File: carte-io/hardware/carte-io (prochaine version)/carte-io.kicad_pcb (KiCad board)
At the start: 4 copper layers, 117.5 x 88.5 mm, 191 parts, among them J1 USB_C_Receptacle_USB2.0_14P, J10 JST_PH_B4B, J11 JST_PH_B4B, J12 JST_PH_B4B, J13 JST_PH_B4B, J14 JST_PH_B4B, J15 JST_PH_B4B, J16 JST_PH_B4B, J17 JST_PH_B4B, J18 JST_PH_B4B, J19 JST_PH_B4B, J2 JST-XH_S2B-XH-A, J20 Conn_02x08_Odd_Even, J22 JST_PH_B6B, J23 JST_PH_B4B, J24 JST_PH_B4B, J25 JST_PH_B4B, J26 JST-PH-B2B, J27 JST_PH_B5B, J3 FTSH-105-01-L-DV-007, J4 JST_PH_B4B, J5 JST_PH_B4B, J6 JST_PH_B4B, J7 JST_PH_B4B, J8 TSW-104-07-G-T, J9 TSW-104-07-G-T, Q1 IRF9388TRPBF, SW1 SW_Push, SW2 SW_Push, U1 STM32U545VETx, U10 CM1293A-04SO, U11 74LVC125APW, U12 LSM6DS3, U13 LIS2MDL, U14 LPS22DF, U15 PCA9544APW, U16 LT1963AxST-3.3, U17 PCA9544APW, U18 APDS-9251-001, U19 SHT4x, U2 FT231XQ, U20 74LVC2G125DP,125, U21 CM1293A-04SO, U22 CM1293A-04SO, U23 74LVC125APW, U24 CM1293A-04SO, U25 74LVC125APW, U26 74LVC2G125DP,125, U27 CM1293A-04SO, U28 74LVC2G125DP,125, U29 CM1293A-04SO, U3 LT1963AxST-3.3, U30 74LVC125APW,118, U31 CM1293A-04SO, U32 74LVC2G125DP,125, U33 MCP2542FDxMF, U34 CM1293A-04SO, U35 TCA9802, U4 CM1293A-04SO, U5 TXU0104PWR, U6 74LVC125APW, U7 CM1293A-04SO, U8 CM1293A-04SO, U9 TXU0104PWR, X1 ASE-16.000MHZ-LC-T

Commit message: Commit de sauvegarde, gros changement sur la carte IO, les connecteurs sont compatibles SeeedStudio Grove. Il faut reprendre une grosse partie du routage et rajouter deux entrées analogiques
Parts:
- removed C39, C40, C41, C43: 100nF, Capacitor_SMD:C_0805_2012Metric_Pad1.18x1.45mm_HandSolder
- removed R36, R37, R38, R39, R44, R47, R48, R49: 100R, Resistor_SMD:R_0805_2012Metric_Pad1.20x1.40mm_HandSolder
- removed U22, U31: CM1293A-04SO, CM1293A-04SO:SOT95P285X140-6N
- removed U23, U25: 74LVC125APW, 74LVC125APW:IC_74LVC125APW
- removed U30: 74LVC125APW,118, Package_SO:TSSOP-14_4.4x5mm_P0.65mm
- added J21: 114020164, SeeedStudio - Horizontal Header -114020164:SEEEDSTUDIO_114020164, F.Cu at (179.0, 155.6)
- added J28: 114020164, SeeedStudio - Horizontal Header -114020164:SEEEDSTUDIO_114020164, F.Cu at (204.1, 155.6)
- added R73: 4.7K, Resistor_SMD:R_0805_2012Metric_Pad1.20x1.40mm_HandSolder, F.Cu at (216.8, 57.8)
- added R74: 4.7K, Resistor_SMD:R_0805_2012Metric_Pad1.20x1.40mm_HandSolder, F.Cu at (216.8, 60.7)
- J10, J12, J14, J16, J18, J19, J23, J24, J25, J4, J5, J6, J7: value JST_PH_B4B -> 114020164; footprint Connector_JST:JST_PH_B4B-PH-K_1x04_P2.00mm_Vertical -> SeeedStudio - Horizontal Header -114020164:SEEEDSTUDIO_114020164
- J11, J13, J15, J17: value JST_PH_B4B -> 114020164; footprint Connector_JST:JST_PH_B4B-PH-K_1x04_P2.00mm_Vertical -> SeeedStudio - Horizontal Header -114020164:SEEEDSTUDIO_114020164; moved to B.Cu
- J2: value JST-XH_S2B-XH-A -> 114020164; footprint Connector_JST:JST_XH_S2B-XH-A_1x02_P2.50mm_Horizontal -> SeeedStudio - Horizontal Header -114020164:SEEEDSTUDIO_114020164
- J20: value Conn_02x08_Odd_Even -> 114020164; footprint Connector_PinHeader_2.54mm:PinHeader_2x07_P2.54mm_Vertical -> SeeedStudio - Horizontal Header -114020164:SEEEDSTUDIO_114020164
- J22: value JST_PH_B6B -> 114020164; footprint Connector_JST:JST_PH_B6B-PH-K_1x06_P2.00mm_Vertical -> SeeedStudio - Horizontal Header -114020164:SEEEDSTUDIO_114020164
- J26: value JST-PH-B2B -> 114020164; footprint Connector_JST:JST_PH_B2B-PH-K_1x02_P2.00mm_Vertical -> SeeedStudio - Horizontal Header -114020164:SEEEDSTUDIO_114020164; moved to B.Cu
- J27: value JST_PH_B5B -> 114020164; footprint Connector_JST:JST_PH_B5B-PH-K_1x05_P2.00mm_Vertical -> SeeedStudio - Horizontal Header -114020164:SEEEDSTUDIO_114020164
- moved J22 51.7 mm to (191.6, 155.6), turned to 90 degrees
- moved J26 42.1 mm to (92.7, 124.2), turned to 90 degrees
- moved J20 19.7 mm to (166.5, 155.6)
- moved J12 7.32 mm to (144.3, 60.4), turned to 180 degrees
- moved J16 7.32 mm to (157.0, 60.4), turned to 180 degrees
- moved J14 7.11 mm to (131.3, 60.4), turned to 180 degrees
- moved J10 6.74 mm to (118.0, 60.4), turned to 180 degrees
- moved J15 6.19 mm to (130.9, 60.2), turned to 0 degrees
- moved J11 6.13 mm to (117.8, 60.4), turned to 0 degrees
- moved J13 5.96 mm to (144.4, 60.2), turned to 0 degrees
- moved U19 5.96 mm to (169.8, 85.5)
- moved J17 5.63 mm to (157.2, 60.5), turned to 0 degrees
- moved J2 2.95 mm to (92.7, 124.2)
- moved R29 1.63 mm to (164.1, 85.3)
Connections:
- J10 pad 1: +3.3V_PWR -> Net-(J10-Pin_1)
- J10 pad 3: GND -> +3.3V_PWR
- J10 pad 4: Net-(J10-Pin_4) -> GND
- J11 pad 1: +3.3V_PWR -> Net-(J11-Pin_1)
- J11 pad 3: GND -> +3.3V_PWR
- J11 pad 4: Net-(J11-Pin_4) -> GND
- J12 pad 1: +3.3V_PWR -> Net-(J12-Pin_1)
- J12 pad 3: GND -> +3.3V_PWR
- J12 pad 4: Net-(J12-Pin_4) -> GND
- J13 pad 1: +3.3V_PWR -> Net-(J13-Pin_1)
- J13 pad 3: GND -> +3.3V_PWR
- J13 pad 4: Net-(J13-Pin_4) -> GND
- J14 pad 1: +3.3V_PWR -> Net-(J14-Pin_1)
- J14 pad 3: GND -> +3.3V_PWR
- J14 pad 4: Net-(J14-Pin_4) -> GND
- J15 pad 1: +3.3V_PWR -> Net-(J15-Pin_1)
- J15 pad 3: GND -> +3.3V_PWR
- J15 pad 4: Net-(J15-Pin_4) -> GND
- J16 pad 1: +3.3V_PWR -> Net-(J16-Pin_1)
- J16 pad 3: GND -> +3.3V_PWR
- J16 pad 4: Net-(J16-Pin_4) -> GND
- J17 pad 1: +3.3V_PWR -> Net-(J17-Pin_1)
- J17 pad 3: GND -> +3.3V_PWR
- J17 pad 4: Net-(J17-Pin_4) -> GND
- J18 pad 1: +5V -> Net-(J18-Pin_1)
- J18 pad 3: GND -> +5V
- J18 pad 4: Net-(J18-Pin_4) -> GND
- J19 pad 1: +5V -> Net-(J19-Pin_1)
- J19 pad 3: GND -> +5V
- J19 pad 4: Net-(J19-Pin_4) -> GND
- J2 pad 1: /Power & Analog/VIN -> GND
- J2 pad 2: GND -> /Power & Analog/VIN
- J20 pad 1: +3.3V_PWR -> /GPIO SPI GEN_PWM/IO1
- J20 pad 2: +5V -> unconnected-(J20-Pin_2-Pad2)
- J20 pad 3: GND -> +3.3V
- J22 pad 1: +3.3V_PWR -> /GPIO SPI GEN_PWM/IO4
- J22 pad 2: /GPIO SPI GEN_PWM/SPI_CS_EXT -> unconnected-(J22-Pin_2-Pad2)
- J22 pad 3: /GPIO SPI GEN_PWM/SPI_CLK_EXT -> +3.3V
- J23 pad 1: +3.3V_PWR -> Net-(J23-Pin_1)
- J23 pad 3: GND -> +3.3V_PWR
- J23 pad 4: Net-(J23-Pin_4) -> GND
- J24 pad 1: +3.3V_PWR -> Net-(J23-Pin_1)
- J24 pad 3: GND -> +3.3V_PWR
- J24 pad 4: Net-(J23-Pin_4) -> GND
- J25 pad 1: +5V -> Net-(J25-Pin_1)
- J25 pad 3: GND -> +5V
- J25 pad 4: Net-(J25-Pin_4) -> GND
- J26 pad 1: GND -> /CPU/~{POWEROFF}
- J26 pad 2: Net-(J26-Pin_2) -> /CPU/PWR_CSLEEP
- J27 pad 1: +5V -> Net-(J27-Pin_1)
- J27 pad 2: +3.3V -> Net-(J27-Pin_2)
- J27 pad 3: Net-(J27-Pin_3) -> +5V
- J4 pad 1: +3.3V -> Net-(J4-Pin_1)
- J4 pad 3: GND -> +3.3V
- J4 pad 4: Net-(J4-Pin_4) -> GND
- J5 pad 1: +3.3V -> Net-(J5-Pin_1)
- J5 pad 3: GND -> +3.3V
- J5 pad 4: Net-(J5-Pin_4) -> GND
- J6 pad 1: +3.3V -> Net-(J6-Pin_1)
- J6 pad 3: GND -> +3.3V
- J6 pad 4: Net-(J6-Pin_4) -> GND
- J7 pad 1: +3.3V -> Net-(J7-Pin_1)
- J7 pad 3: GND -> +3.3V
- J7 pad 4: Net-(J7-Pin_4) -> GND
- R11 pad 1: Net-(J4-Pin_2) -> Net-(J4-Pin_1)
- R12 pad 1: Net-(J4-Pin_4) -> Net-(J4-Pin_2)
- R13 pad 1: Net-(J5-Pin_2) -> Net-(J5-Pin_1)
- R14 pad 1: Net-(J5-Pin_4) -> Net-(J5-Pin_2)
- R19 pad 1: Net-(J6-Pin_2) -> Net-(J6-Pin_1)
- R20 pad 1: Net-(J6-Pin_4) -> Net-(J6-Pin_2)
- R21 pad 1: Net-(J7-Pin_2) -> Net-(J7-Pin_1)
- R22 pad 1: Net-(J7-Pin_4) -> Net-(J7-Pin_2)
- R32 pad 2: Net-(J18-Pin_4) -> Net-(J18-Pin_1)
- R34 pad 2: Net-(J19-Pin_4) -> Net-(J19-Pin_1)
- R35 pad 2: Net-(J25-Pin_4) -> Net-(J25-Pin_1)
- R40 pad 1: Net-(U23-1Y) -> /CPU/IO1
- R40 pad 2: /GPIO SPI GEN_PWM/OUT1 -> /GPIO SPI GEN_PWM/IO1
- R41 pad 1: Net-(U23-2Y) -> /CPU/IO2
- R41 pad 2: /GPIO SPI GEN_PWM/OUT2 -> /GPIO SPI GEN_PWM/IO2
- R42 pad 1: Net-(U23-3Y) -> /CPU/IO3
- R42 pad 2: /GPIO SPI GEN_PWM/OUT3 -> /GPIO SPI GEN_PWM/IO3
- R43 pad 1: Net-(U23-4Y) -> /CPU/IO4
- R43 pad 2: /GPIO SPI GEN_PWM/OUT4 -> /GPIO SPI GEN_PWM/IO4
- R45 pad 2: Net-(J27-Pin_3) -> Net-(J27-Pin_2)
- R46 pad 2: Net-(J27-Pin_5) -> Net-(J27-Pin_1)
- R52 pad 1: Net-(J26-Pin_2) -> Net-(J26-Pin_3)
- R57 pad 2: Net-(J10-Pin_4) -> Net-(J10-Pin_1)
- R59 pad 2: Net-(J14-Pin_4) -> Net-(J14-Pin_1)
- R61 pad 2: Net-(J15-Pin_4) -> Net-(J15-Pin_1)
- R62 pad 1: Net-(J11-Pin_4) -> Net-(J11-Pin_1)
- R65 pad 2: Net-(J12-Pin_4) -> Net-(J12-Pin_1)
- R67 pad 2: Net-(J16-Pin_4) -> Net-(J16-Pin_1)
- R69 pad 2: Net-(J17-Pin_4) -> Net-(J17-Pin_1)
- R70 pad 1: Net-(J13-Pin_4) -> Net-(J13-Pin_1)
- U1 pad 31: /CPU/SPI_MISO -> unconnected-(U1-PA6-Pad31)
- U1 pad 32: /CPU/SPI_MOSI -> unconnected-(U1-PA7-Pad32)
- U1 pad 38: /CPU/INPUT1 -> /CPU/IO1
- U1 pad 39: /CPU/INPUT2 -> /CPU/IO2
- U1 pad 40: /CPU/INPUT3 -> /CPU/IO3
- U1 pad 41: /CPU/INPUT4 -> /CPU/IO4
- U1 pad 42: /CPU/OUTPUT1 -> unconnected-(U1-PE11-Pad42)
- U1 pad 43: /CPU/OUTPUT2 -> unconnected-(U1-PE12-Pad43)
- U1 pad 44: /CPU/SPI_SCK -> unconnected-(U1-PE13-Pad44)
- U1 pad 45: /CPU/OUTPUT3 -> unconnected-(U1-PE14-Pad45)
- U1 pad 46: /CPU/OUTPUT4 -> unconnected-(U1-PE15-Pad46)
- U1 pad 97: /CPU/SPI_CS -> unconnected-(U1-PE0-Pad97)
- U15 pad 13: Net-(J11-Pin_4) -> Net-(J11-Pin_1)
- U15 pad 16: Net-(J15-Pin_4) -> Net-(J15-Pin_1)
- U15 pad 6: Net-(J10-Pin_4) -> Net-(J10-Pin_1)
- U15 pad 9: Net-(J14-Pin_4) -> Net-(J14-Pin_1)
- U17 pad 13: Net-(J13-Pin_4) -> Net-(J13-Pin_1)
- U17 pad 16: Net-(J17-Pin_4) -> Net-(J17-Pin_1)
- U17 pad 6: Net-(J12-Pin_4) -> Net-(J12-Pin_1)
- U17 pad 9: Net-(J16-Pin_4) -> Net-(J16-Pin_1)
- U21 pad 5: +5V -> +3.3V
- U24 pad 1: Net-(U23-1Y) -> /CPU/IO1
- U24 pad 3: Net-(U23-2Y) -> /CPU/IO2
- U24 pad 4: Net-(U23-3Y) -> /CPU/IO3
- U24 pad 6: Net-(U23-4Y) -> /CPU/IO4
- U27 pad 5: +5V -> +3.3V
- U29 pad 5: +5V -> +3.3V
- U33 pad 6: Net-(J25-Pin_4) -> Net-(J25-Pin_1)
- U35 pad 7: Net-(J23-Pin_4) -> Net-(J23-Pin_1)
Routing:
- net (no net): track 0.00 -> 326.6 mm, vias 0 -> 9
- net /CPU/IO4: track 0.00 -> 88.5 mm, vias 0 -> 5
- net /CPU/IO2: track 0.00 -> 85.8 mm, vias 0 -> 2
- net /CPU/IO3: track 0.00 -> 85.3 mm, vias 0 -> 5
- net /CPU/IO1: track 0.00 -> 83.1 mm, vias 0 -> 4
- net GND: track 447.9 -> 530.1 mm, vias 63 -> 70
- net unconnected-(U1-PA6-Pad31): track 0.00 -> 57.4 mm, vias 0 -> 4
- net /CPU/SPI_MISO: track 57.4 -> 0.00 mm, vias 4 -> 0
- net /CPU/INPUT2: track 56.9 -> 0.00 mm, vias 2 -> 0
- net /CPU/INPUT1: track 55.2 -> 0.00 mm, vias 2 -> 0
- net unconnected-(U1-PE0-Pad97): track 0.00 -> 54.8 mm, vias 0 -> 4
- net /CPU/SPI_CS: track 54.8 -> 0.00 mm, vias 4 -> 0
- net /CPU/INPUT3: track 52.3 -> 0.00 mm, vias 2 -> 0
- net unconnected-(U1-PA7-Pad32): track 0.00 -> 51.3 mm, vias 0 -> 4
- net /CPU/SPI_MOSI: track 51.3 -> 0.00 mm, vias 4 -> 0
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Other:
- outline, holes or cut-outs redrawn

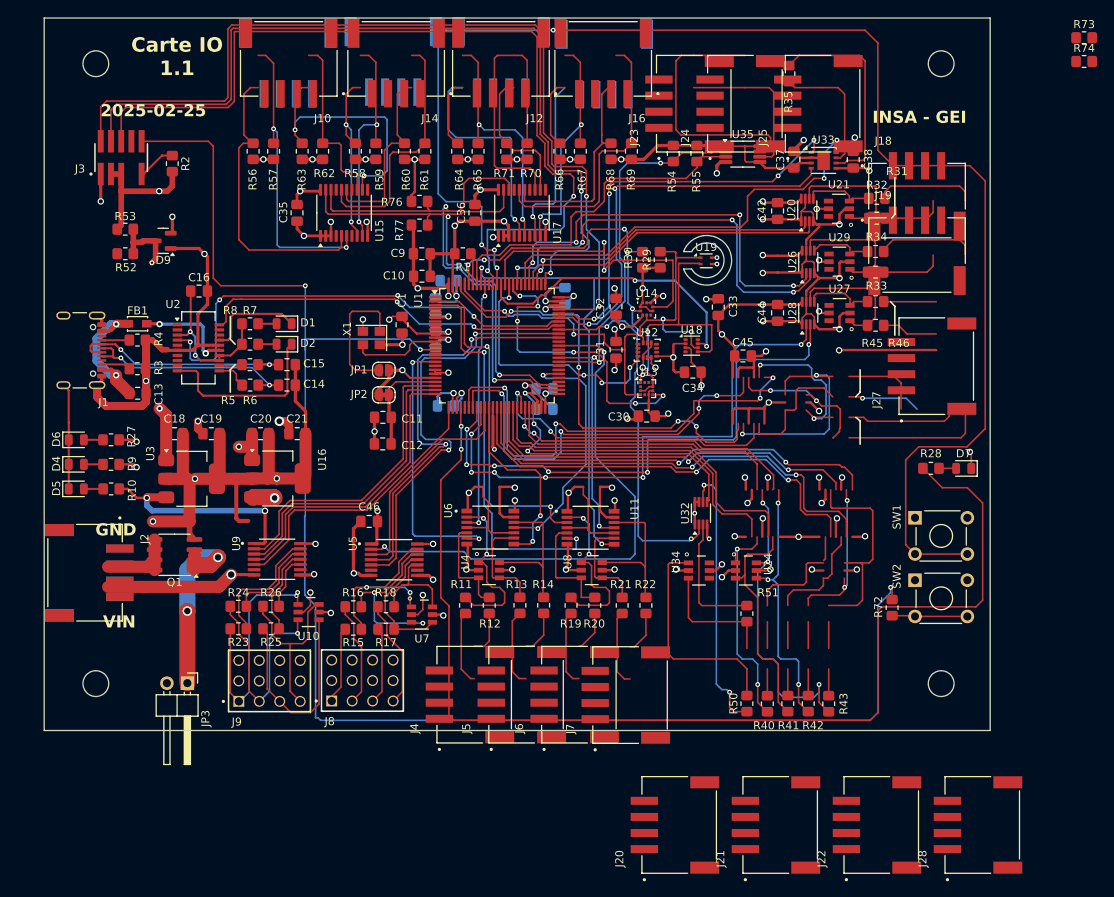
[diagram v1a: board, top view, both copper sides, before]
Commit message: -- reorganisation de la carte, - rajout des connecteurs seeedstudio grove - Rajout des deux entrées ADC
travail en cours
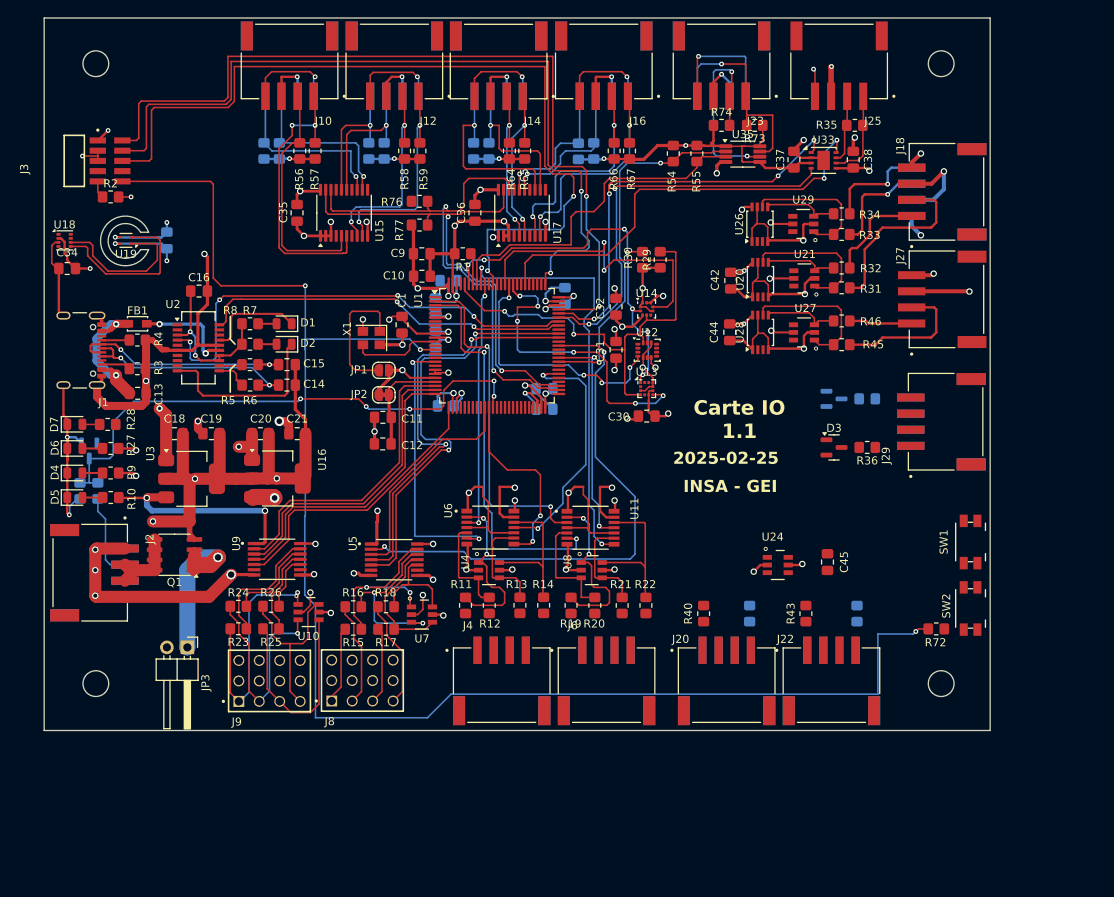
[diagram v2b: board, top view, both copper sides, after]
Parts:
- removed C46: 100nF, Capacitor_SMD:C_0805_2012Metric_Pad1.18x1.45mm_HandSolder
- removed R50, R51: 100R, Resistor_SMD:R_0805_2012Metric_Pad1.20x1.40mm_HandSolder
- removed U32: 74LVC2G125DP,125, Package_SO:VSSOP-8_2.3x2mm_P0.5mm
- removed U34: CM1293A-04SO, CM1293A-04SO:SOT95P285X140-6N
- added D3: BAT54SFILMY, Package_TO_SOT_SMD:SOT-23, F.Cu at (185.7, 108.7)
- added D8: BAT54SFILMY, Package_TO_SOT_SMD:SOT-23, B.Cu at (185.7, 102.6)
- added J29: 114020164, SeeedStudio - Horizontal Header -114020164:SEEEDSTUDIO_114020164, F.Cu at (199.5, 105.5)
- added J30: 114020164, SeeedStudio - Horizontal Header -114020164:SEEEDSTUDIO_114020164, B.Cu at (199.5, 105.5)
- added R36: 100R, Resistor_SMD:R_0805_2012Metric_Pad1.20x1.40mm_HandSolder, F.Cu at (189.8, 108.7)
- added R37: 100R, Resistor_SMD:R_0805_2012Metric_Pad1.20x1.40mm_HandSolder, B.Cu at (189.8, 102.6)
- C33, D9, J19, J21, J24, J28, J5, J7, R41, R42, R52, R53, R60, R61, R62, R63, R68, R69, R70, R71: moved to B.Cu
- J3: value FTSH-105-01-L-DV-007 -> FTSH-105-01-L-DH; footprint FTSH-105-01-L-DV-007-K:SAMTEC_FTSH-105-X-X-DV-007-P-X -> FTSH-105-01-L-DH:SAMTEC_FTSH-105-01-L-DH
- SW1, SW2: footprint Button_Switch_THT:SW_TH_Tactile_Omron_B3F-10xx -> Button_Switch_SMD:Panasonic_EVQPUJ_EVQPUA
- U20, U26, U28: footprint Package_SO:VSSOP-8_2.3x2mm_P0.5mm -> Package_SO:TSSOP-8_3x3mm_P0.65mm
- moved D7 110.5 mm to (91.4, 105.8), turned to 0 degrees
- moved R28 102.4 mm to (95.5, 105.8), turned to 180 degrees
- moved U18 79.0 mm to (90.1, 82.9)
- moved C34 78.8 mm to (90.4, 86.4), turned to 180 degrees
- moved U19 72.1 mm to (97.7, 82.9), turned to 180 degrees
- moved C33 69.0 mm to (102.8, 82.9), turned to -90 degrees
- moved R74 45.7 mm to (171.7, 68.7)
- moved R73 42.3 mm to (175.8, 68.7), turned to 180 degrees
- moved R53 33.0 mm to (92.0, 114.1), turned to -90 degrees
- moved R52 29.7 mm to (94.2, 114.1), turned to 90 degrees
- moved D9 27.7 mm to (93.2, 109.1), turned to -90 degrees
- moved C45 27.7 mm to (184.9, 122.9), turned to 90 degrees
- moved J28 25.5 mm to (185.4, 138.2), turned to 180 degrees
- moved J21 18.6 mm to (172.4, 138.2), turned to 180 degrees
- moved J22 18.4 mm to (185.4, 138.2), turned to 0 degrees
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- renumbered J14 to J12, J15 to J13, J12 to J14, J13 to J15
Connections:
- U1 pad 43: unconnected-(U1-PE12-Pad43) -> /CPU/ADC_AN1
- U1 pad 44: unconnected-(U1-PE13-Pad44) -> /CPU/ADC_AN2
- U1 pad 47: /CPU/GEN_PWM2 -> unconnected-(U1-PB10-Pad47)
- U1 pad 67: /CPU/GEN_PWM1 -> unconnected-(U1-PA8-Pad67)
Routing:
- net (no net): track 326.6 -> 0.00 mm, vias 9 -> 0
- net /CPU/USER_BTN: track 181.2 -> 0.00 mm, vias 4 -> 0
- net /CPU/LED_ACTIVITY: track 141.2 -> 0.00 mm, vias 2 -> 0
- net +3.3V_PWR: track 227.5 -> 125.0 mm, vias 3 -> 8
- net /CPU/IO4: track 88.5 -> 0.00 mm, vias 5 -> 0
- net /CPU/IO2: track 85.8 -> 0.00 mm, vias 2 -> 0
- net /CPU/IO3: track 85.3 -> 0.00 mm, vias 5 -> 0
- net /CPU/IO1: track 83.1 -> 0.00 mm, vias 4 -> 0
- net /CPU/COM_GPS_RX: track 68.6 -> 0.00 mm, vias 6 -> 0
- net GND: track 530.1 -> 461.7 mm, vias 70 -> 60
- net /CPU/COM_GPS_TX: track 68.3 -> 0.00 mm, vias 6 -> 0
- net unconnected-(U1-PA6-Pad31): track 57.4 -> 0.00 mm, vias 4 -> 0
- net unconnected-(U1-PE0-Pad97): track 54.8 -> 0.00 mm, vias 4 -> 0
- net /CPU/COM_LIDAR2_RX: track 52.7 -> 0.00 mm, vias 4 -> 0
- net /CPU/COM_LIDAR2_TX: track 51.4 -> 0.00 mm, vias 4 -> 0
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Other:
- outline, holes or cut-outs redrawn
- board text removed: "GND"
- board text removed: "VIN"

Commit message: WIP
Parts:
- added C43: 100nF, Capacitor_SMD:C_0805_2012Metric_Pad1.18x1.45mm_HandSolder, F.Cu at (172.7, 80.7)
- R13, R14, R21, R22: moved to B.Cu
- moved C45 6.92 mm to (178.7, 119.8), turned to 180 degrees
- moved R14 4.26 mm to (145.4, 128.3)
- moved R22 3.94 mm to (158.4, 128.3)
- moved C30 3.26 mm to (165.7, 104.8)
- moved C31 3.17 mm to (161.8, 96.5)
- moved C32 3.17 mm to (161.8, 91.2)
- moved R29 3.17 mm to (167.3, 85.3)
- moved R30 3.17 mm to (165.1, 85.3)
- moved U12 3.17 mm to (165.7, 96.6)
- moved U13 3.17 mm to (165.6, 101.4)
- moved U14 3.17 mm to (165.6, 91.5)
- moved R11 1.32 mm to (141.2, 128.3)
- moved R19 1.23 mm to (154.3, 128.3)
- moved R21 1.23 mm to (160.6, 128.3)
- moved R40 0.95 mm to (169.5, 128.3)
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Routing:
- net GND: track 461.7 -> 558.3 mm, vias 60 -> 78
- net /CPU/USER_BTN: track 0.00 -> 95.4 mm, vias 0 -> 4
- net +3.3V: track 308.6 -> 397.4 mm, vias 44 -> 52
- net /CPU/~{POWEROFF}: track 0.00 -> 84.8 mm, vias 0 -> 3
- net /CPU/INT_LIGHT: track 0.00 -> 71.3 mm, vias 0 -> 6
- net /CPU/IO2: track 0.00 -> 67.2 mm, vias 0 -> 2
- net /CPU/I2C_SCL_INT: track 71.1 -> 137.5 mm, vias 7 -> 8
- net /CPU/IO3: track 0.00 -> 63.4 mm, vias 0 -> 2
- net /CPU/IO4: track 0.00 -> 61.2 mm
- net /CPU/PWR_CSLEEP: track 0.00 -> 61.0 mm, vias 0 -> 5
- net /CPU/I2C_SDA_INT: track 73.0 -> 131.6 mm, vias 2 -> 5
- net /CPU/IO1: track 0.00 -> 56.6 mm
- net /CPU/COM_GPS_TX: track 0.00 -> 55.7 mm, vias 0 -> 2
- net /CPU/ADC_AN2: track 0.00 -> 54.4 mm, vias 0 -> 1
- net /CPU/COM_GPS_RX: track 0.00 -> 51.0 mm, vias 0 -> 2
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
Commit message: Carte version 1.1 terminée
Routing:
- net +5V: track 213.6 -> 201.0 mm
- net /CPU/NRST: track 191.8 -> 186.8 mm
- net /CPU/COM_LIDAR1_TX: track 35.9 -> 33.7 mm
- net /CPU/ENCODER_4_PHA: track 52.8 -> 50.8 mm
- net Net-(U4-CH4): track 20.8 -> 19.2 mm
- net /CPU/~{POWEROFF}: track 84.8 -> 83.3 mm
- net GND: track 558.3 -> 556.9 mm
- net +3.3V: track 397.4 -> 398.7 mm
- net Net-(J17-Pin_2): track 18.5 -> 19.6 mm
- net Net-(J17-Pin_1): track 17.7 -> 18.8 mm
- net /CPU/I2C_SDA_INT: track 131.6 -> 132.4 mm

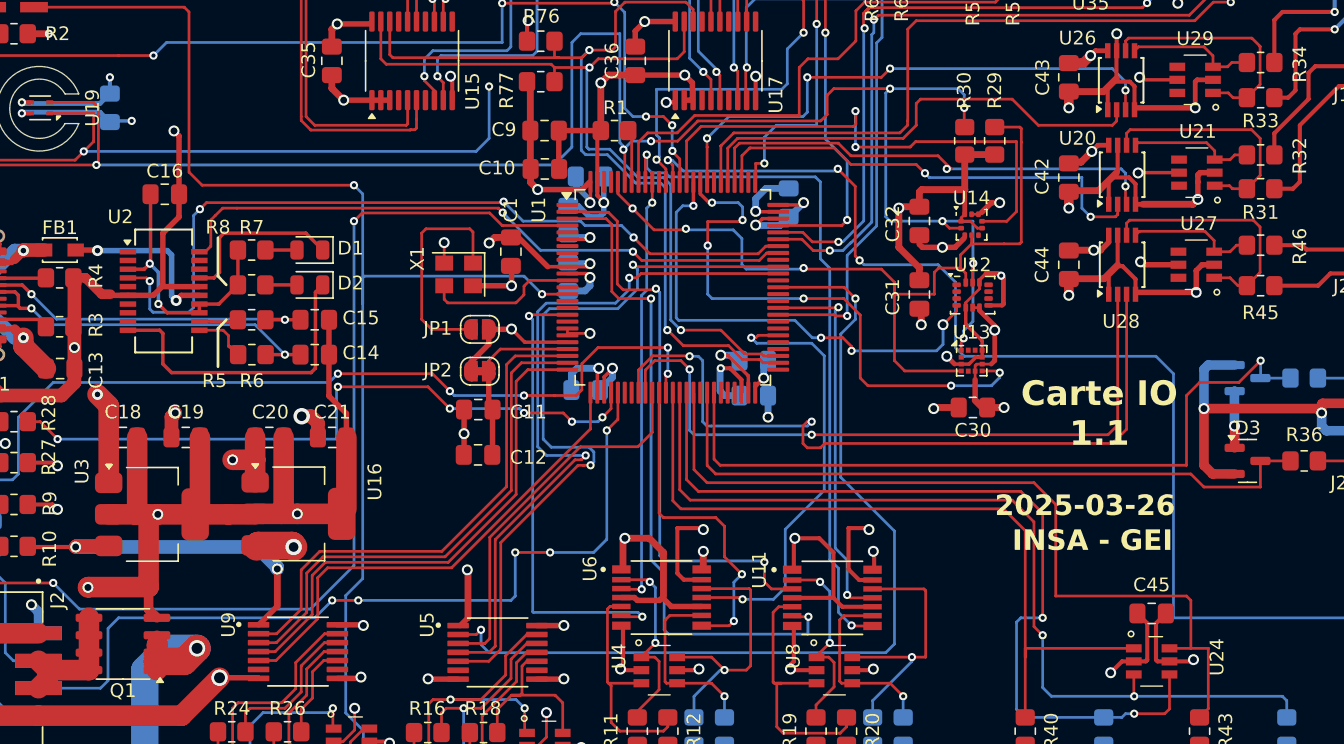
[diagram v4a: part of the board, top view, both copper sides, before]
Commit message: WIP ajout du driver uart (marche) et du driver I2C (juste generé par chatgpt, à reprendre et tester)
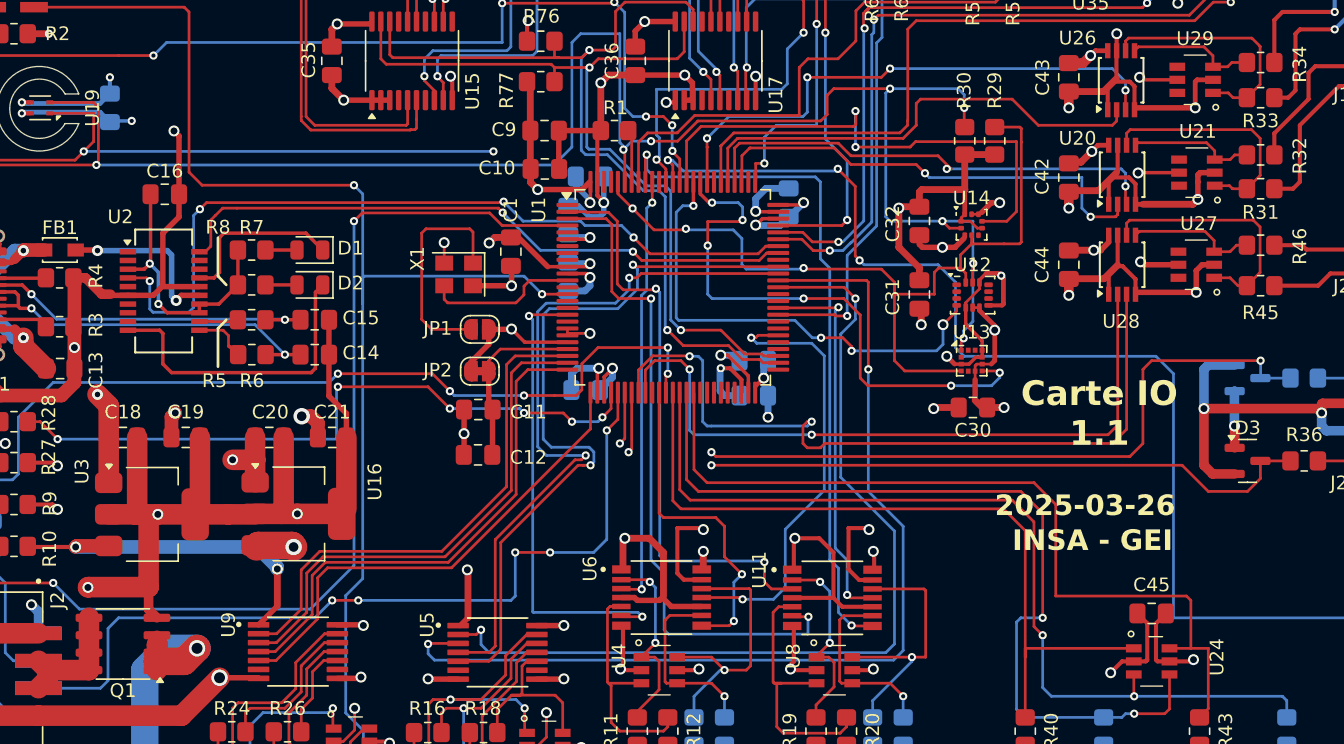
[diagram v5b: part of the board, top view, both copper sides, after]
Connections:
- U1 pad 31: unconnected-(U1-PA6-Pad31) -> /CPU/ADC_AN1
- U1 pad 32: unconnected-(U1-PA7-Pad32) -> /CPU/ADC_AN2
- U1 pad 35: /CPU/SERVO_PWM2N -> unconnected-(U1-PB0-Pad35)
- U1 pad 43: /CPU/ADC_AN1 -> unconnected-(U1-PE12-Pad43)
- U1 pad 44: /CPU/ADC_AN2 -> unconnected-(U1-PE13-Pad44)
- U1 pad 64: unconnected-(U1-PC7-Pad64) -> /CPU/SERVO_PWM2
- U5 pad 3: /CPU/SERVO_PWM2N -> /CPU/SERVO_PWM2
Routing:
- net /CPU/SERVO_PWM2: track 0.00 -> 72.5 mm, vias 0 -> 2
- net /CPU/SERVO_PWM2N: track 27.7 -> 0.00 mm
- net /CPU/I2C_SDA_INT: track 132.4 -> 122.2 mm
- net /CPU/ADC_AN1: track 50.3 -> 56.6 mm, vias 0 -> 2
- net /CPU/ADC_AN2: track 54.4 -> 60.1 mm, vias 1 -> 3
